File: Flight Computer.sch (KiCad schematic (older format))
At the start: 18 parts, among them J1 Conn_01x08, U1 VXO7803-1000, U2 W25Q32JVSS, U3 W25Q32JVSS, U4 Adafruit_GPS_THT, U5 BMP280

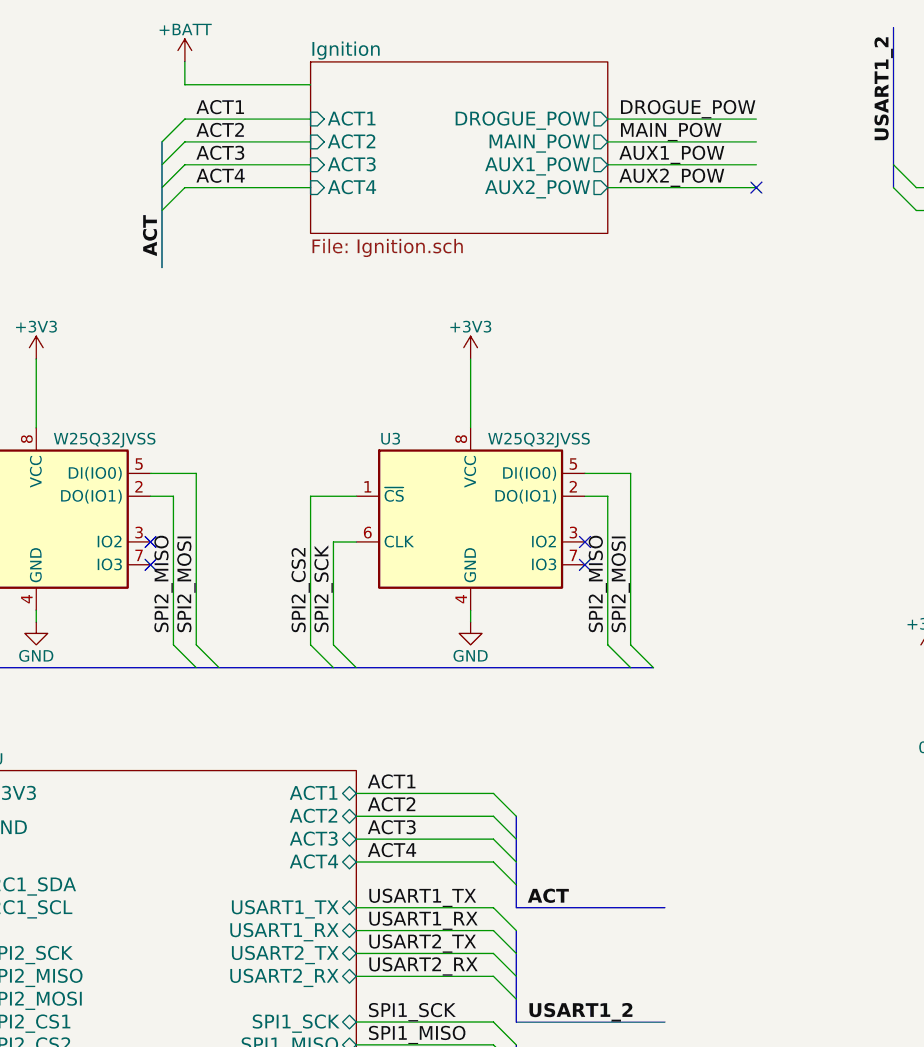
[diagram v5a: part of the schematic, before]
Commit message: Removed redundant ADC protection diodes Basic PCB component layout
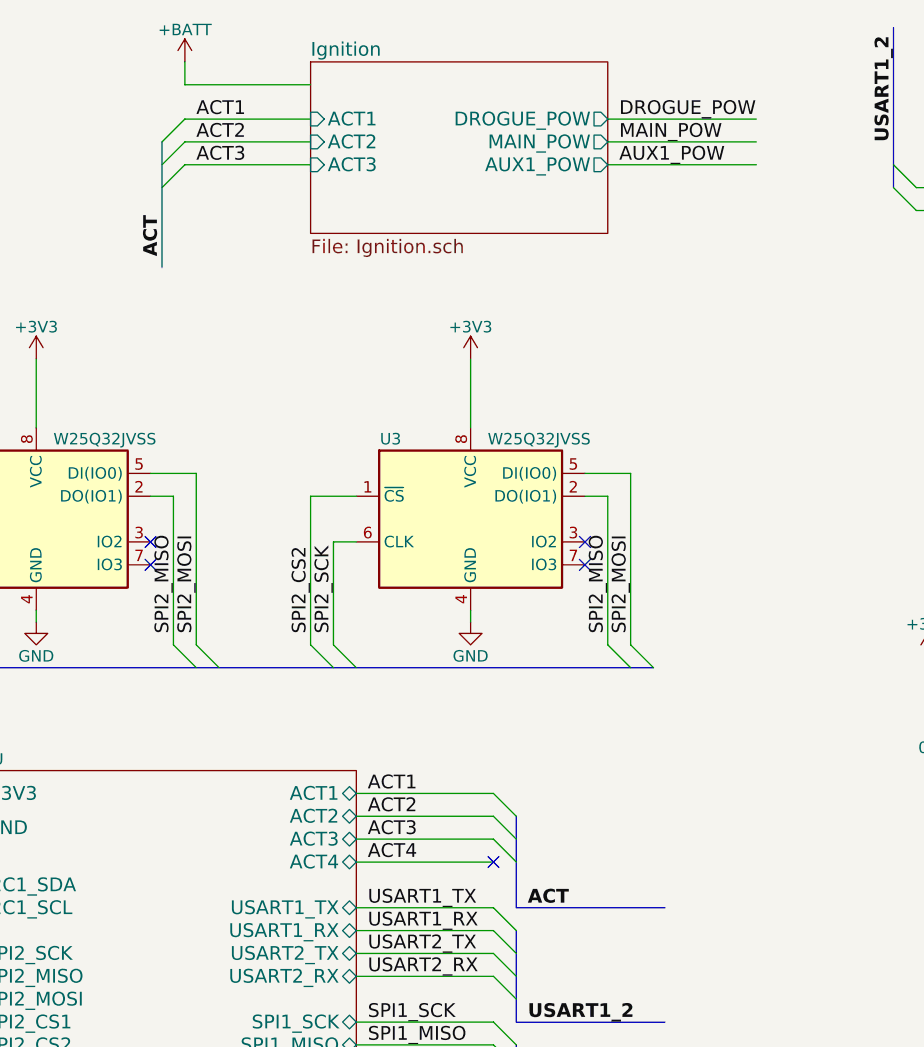
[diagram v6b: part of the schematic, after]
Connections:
- net labels removed: AUX2_POW
- wire segments 148 -> 146
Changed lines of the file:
@@
 F5 "MAIN_POW" O R 5250 3150 60
 F6 "ACT3" I L 3950 3250 60
-F7 "ACT4" I L 3950 3350 60
-F8 "AUX1_POW" O R 5250 3250 60
-F9 "AUX2_POW" O R 5250 3350 60
+F7 "AUX1_POW" O R 5250 3250 60
 $EndSheet
 $Comp
@@
 Wire Wire Line
 	5250 3250 5900 3250
-Wire Wire Line
-	5250 3350 5900 3350
 Text Label 5300 3250 0    60   ~ 0
 AUX1_POW
-Text Label 5300 3350 0    60   ~ 0
-AUX2_POW
 Wire Wire Line
 	3400 3250 3950 3250
-Wire Wire Line
-	3400 3350 3950 3350
 Text Label 3450 3250 0    60   ~ 0
 ACT3
-Text Label 3450 3350 0    60   ~ 0
-ACT4
 Text Label 8650 3400 0    60   ~ 0
 MAIN_POW
@@
 	3300 3350 3400 3250
 Entry Wire Line
-	3300 3450 3400 3350
-NoConn ~ 5900 3350
-Entry Wire Line
 	1350 2300 1450 2200
 Entry Wire Line
@@
 	4750 6200 4850 6300
 Entry Wire Line
-	4750 6300 4850 6400
-Entry Wire Line
 	4750 6500 4850 6600
 Entry Wire Line
@@
 Wire Wire Line
 	4650 4100 4650 4400
+NoConn ~ 4750 6300
 Wire Bus Line
 	7400 5650 7400 6350
@@
 	6500 2650 6500 3350
 Wire Bus Line
+	3300 3150 3300 3700
+Wire Bus Line
+	4850 6100 4850 6500
+Wire Bus Line
 	4850 7100 4850 7800
 Wire Bus Line
 	4850 6600 4850 7000
 Wire Bus Line
-	4850 6100 4850 6500
-Wire Bus Line
-	3300 3150 3300 3700
-Wire Bus Line
 	1450 6800 1450 7300

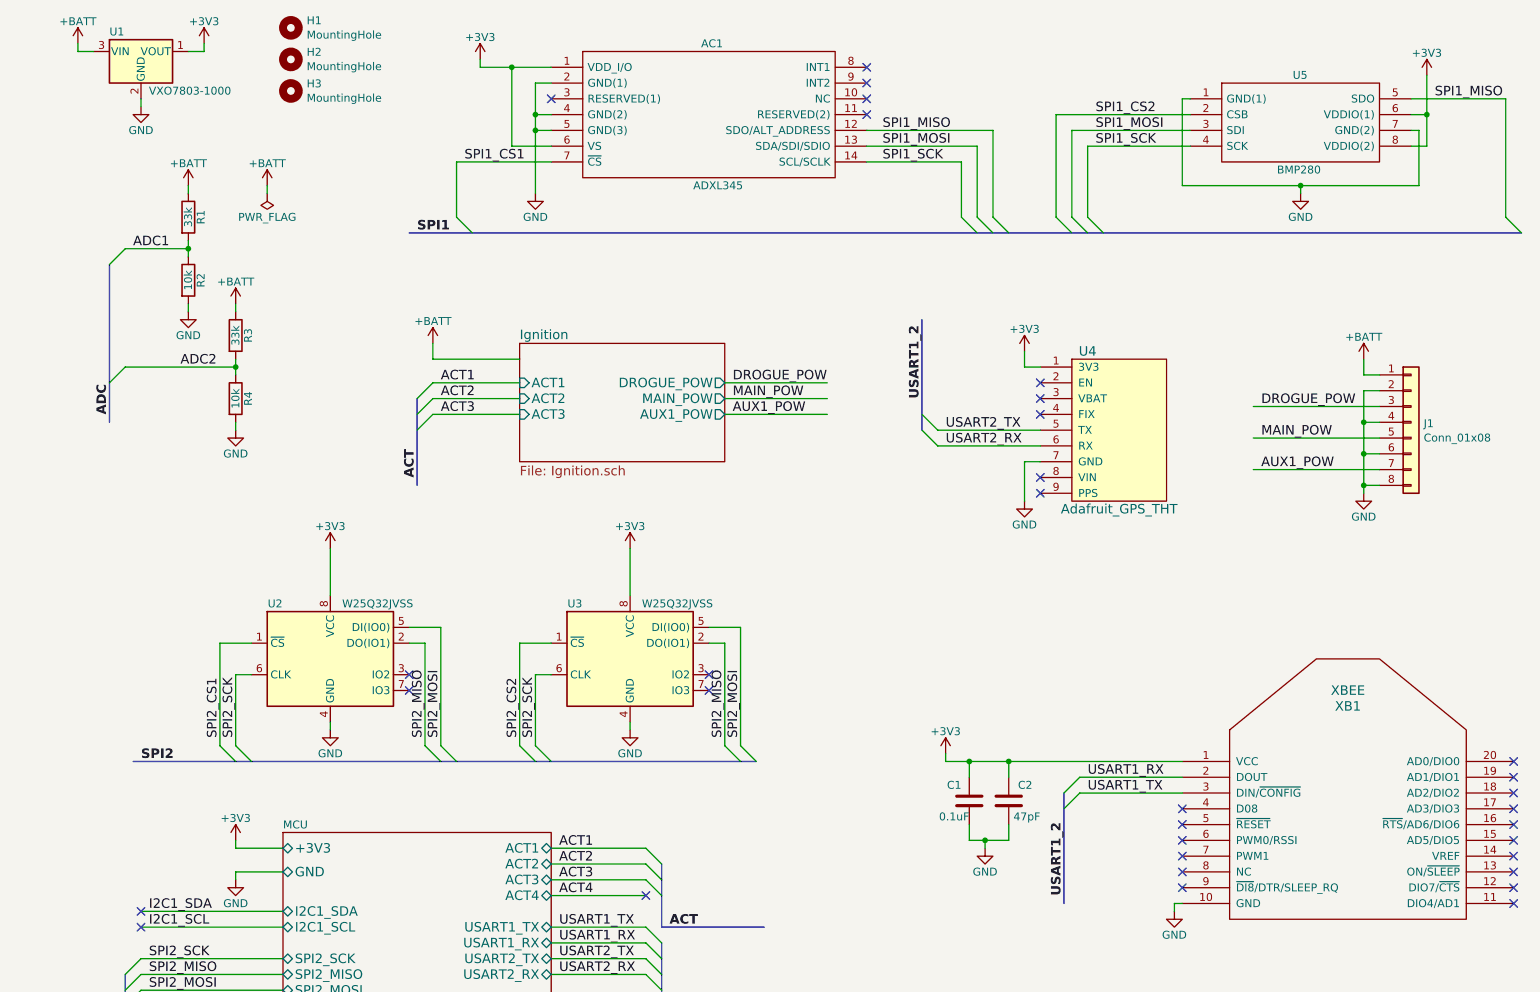
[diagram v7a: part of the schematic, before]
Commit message: Fixed .gitmodules (host-agnostic) Added bypass caps Added NMOS to ignition sheet Added current-limiting resistors Fixed 3V3 ADC input
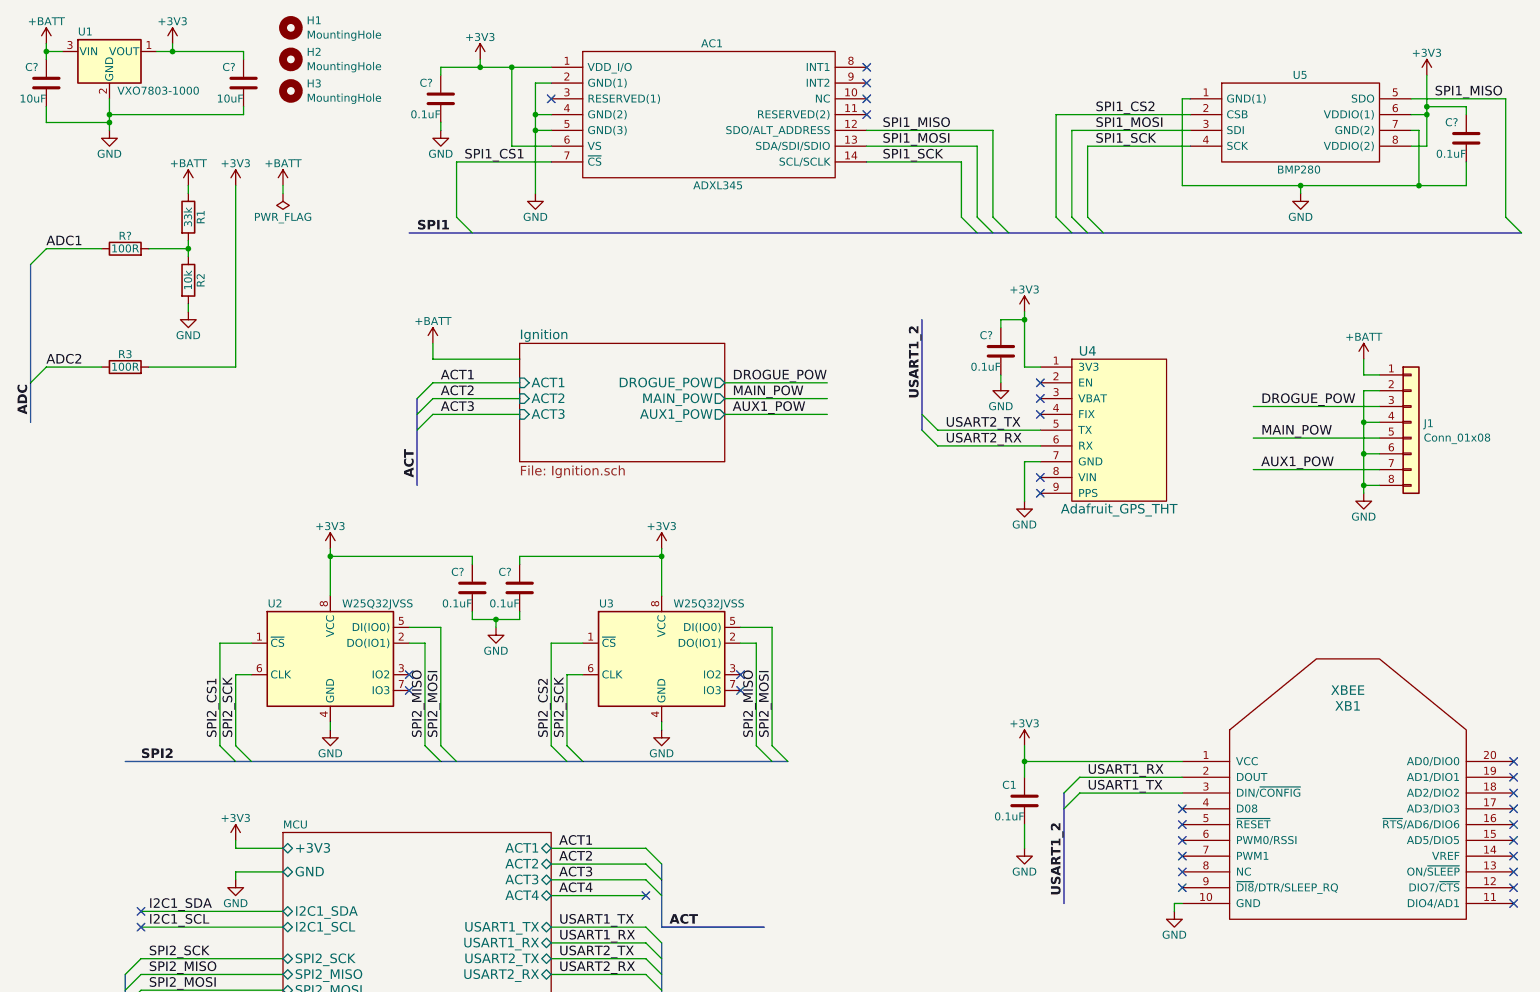
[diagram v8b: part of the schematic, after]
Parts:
- removed C2: 47pF, Capacitor_SMD:C_1206_3216Metric_Pad1.42x1.75mm_HandSolder, symbol Device:C
- removed R4: 10k, Resistor_SMD:R_1206_3216Metric_Pad1.42x1.75mm_HandSolder, symbol Device:R
- added C? (x5): 0.1uF, Capacitor_SMD:C_0603_1608Metric_Pad1.05x0.95mm_HandSolder, symbol Device:C
- added C? (x2): 10uF, Capacitor_SMD:C_1206_3216Metric_Pad1.42x1.75mm_HandSolder, symbol Device:C
- added R?: 100R, Resistor_SMD:R_1206_3216Metric_Pad1.42x1.75mm_HandSolder, symbol Device:R
- C1: footprint Capacitor_SMD:C_1206_3216Metric_Pad1.42x1.75mm_HandSolder -> Capacitor_SMD:C_0603_1608Metric_Pad1.05x0.95mm_HandSolder
- R3: value 33k -> 100R
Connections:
- wire segments 146 -> 170
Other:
- moved on the sheet: C1, R3, U1, U3
